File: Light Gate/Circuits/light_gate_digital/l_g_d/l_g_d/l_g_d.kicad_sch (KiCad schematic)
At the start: 12 parts, among them J1 Conn_01x03_Female, Q1 Q_Photo_NPN_CE, U1 LM393P

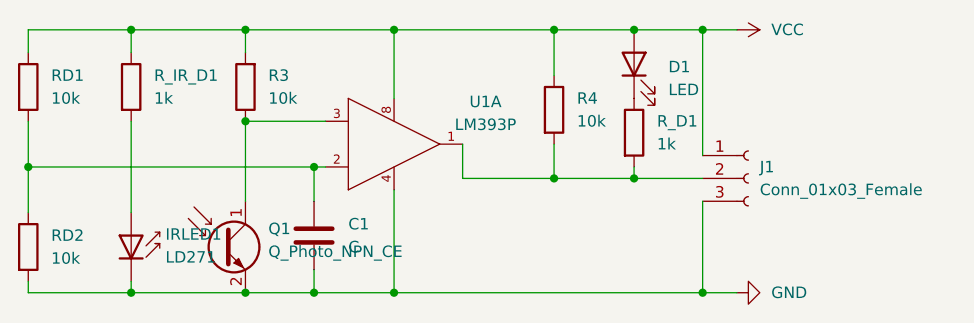
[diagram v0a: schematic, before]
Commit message: changed resistor
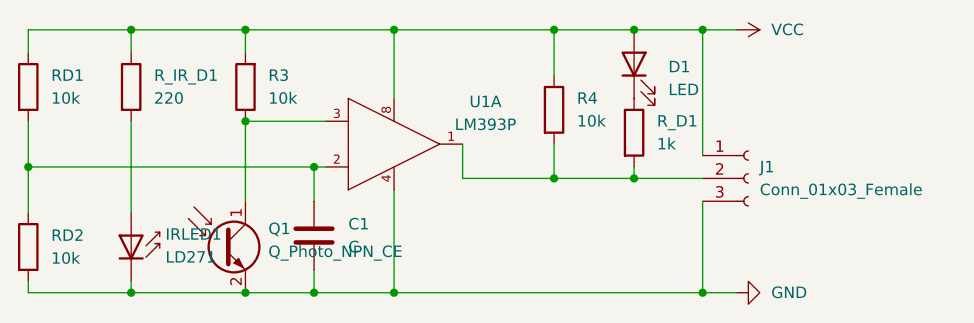
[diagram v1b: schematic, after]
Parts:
- R_IR_D1: value 1k -> 220
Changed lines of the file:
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@@
       (effects (font (size 1.27 1.27)) (justify left))
     )
-    (property "Value" "1k" (id 1) (at 114.3 74.9299 0)
+    (property "Value" "220" (id 1) (at 114.3 74.9299 0)
       (effects (font (size 1.27 1.27)) (justify left))
     )
@@
     )
     (path "/fbde843f-b9b4-48bb-ab60-be1fb10994a4"
-      (reference "R_IR_D1") (unit 1) (value "1k") (footprint "Resistor_THT:R_Axial_DIN0207_L6.3mm_D2.5mm_P7.62mm_Horizontal")
+      (reference "R_IR_D1") (unit 1) (value "220") (footprint "Resistor_THT:R_Axial_DIN0207_L6.3mm_D2.5mm_P7.62mm_Horizontal")
     )
     (path "/b3908863-1f0b-4105-aa33-a8468a4f004e"
